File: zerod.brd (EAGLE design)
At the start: 100 x 80 mm, 34 parts, among them IC1 NE5532N, IC2 LM3914N, Q1 2N3906

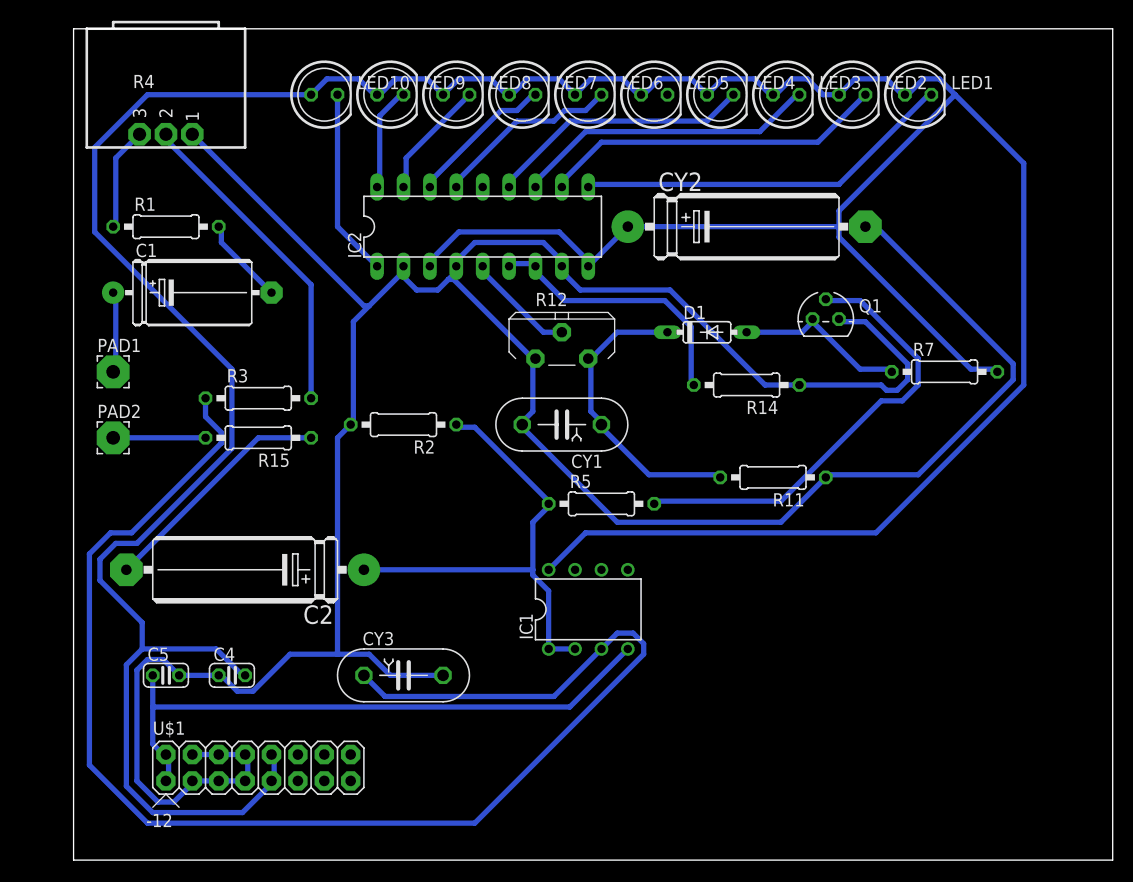
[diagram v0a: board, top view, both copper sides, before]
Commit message: routed board to match updated schematic
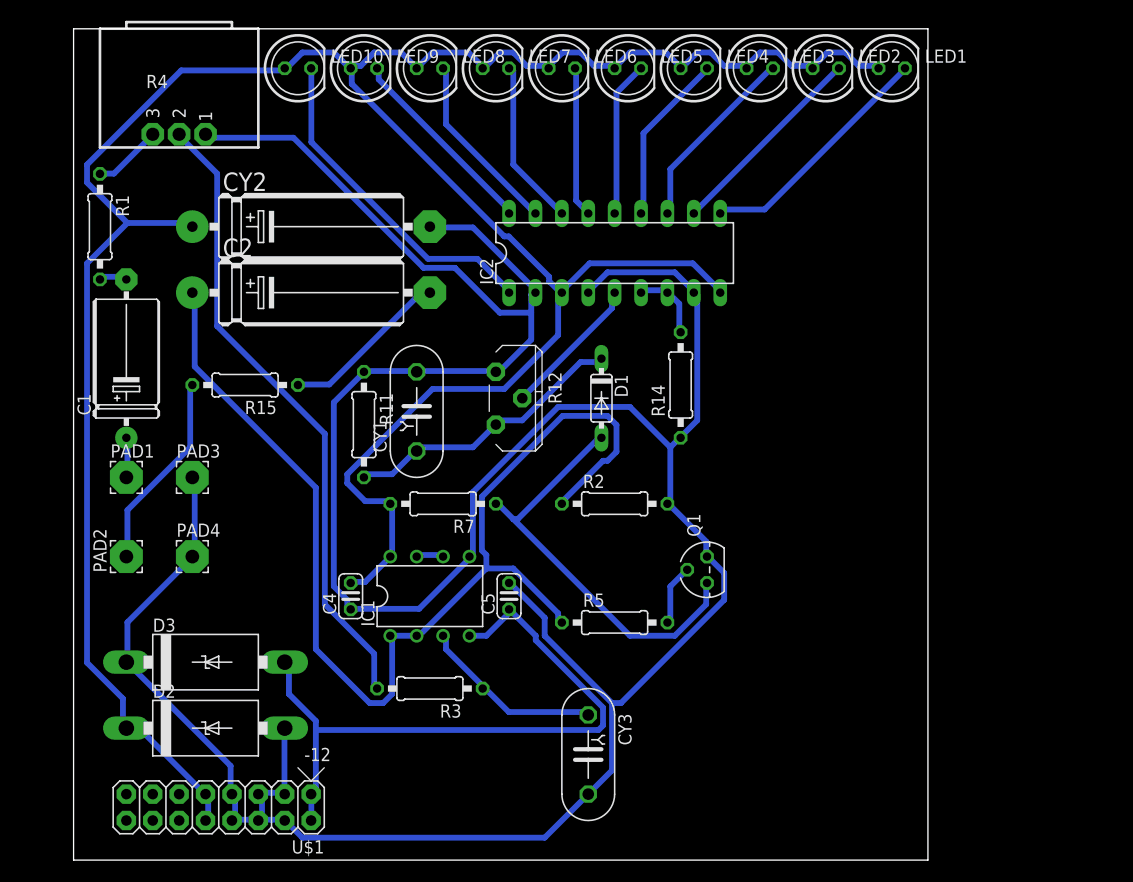
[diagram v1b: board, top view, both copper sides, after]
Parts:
- added D2, D3: 1N5908, diode:C4111-15
- added PAD3: input, wirepad:3,17/1,3
- added PAD4: output, wirepad:3,17/1,3
- moved R7 49.9 mm to (35.6, 34.3), turned to 180 degrees
- moved CY2 41.9 mm to (22.9, 61.0)
- moved R11 39.7 mm to (27.9, 41.9), turned to 270 degrees
- moved C5 33.9 mm to (41.9, 25.4), turned to 90 degrees
- moved R3 32.5 mm to (34.3, 16.5), turned to 180 degrees
- moved C2 27.4 mm to (22.9, 54.6), turned to 0 degrees
- moved Q1 26.7 mm to (61.0, 27.9), turned to 90 degrees
- moved R2 21.7 mm to (52.1, 34.3), turned to 0 degrees
- moved CY3 19.3 mm to (49.5, 10.2), turned to 270 degrees
- moved IC1 15.3 mm to (34.3, 25.4)
- moved CY1 14.0 mm to (33.0, 43.2), turned to 90 degrees
- moved C4 13.7 mm to (26.7, 25.4), turned to 90 degrees
- moved IC2 13.0 mm to (52.1, 58.4)
- moved D1 12.0 mm to (50.8, 44.5), turned to 270 degrees
- moved PAD2 11.5 mm to (5.08, 29.2), turned to 90 degrees
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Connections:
- new net N$24: IC1.6, IC1.7
- net +12V: now also D2.C
- net -12V: now also D3.A
- net GNDA: now also D2.A, D3.C, IC1.5, PAD3.1, PAD4.1
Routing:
- net N$6: track 136.5 -> 18.0 mm
- net +12V: track 370.8 -> 264.4 mm
- net N$5: track 46.2 -> 110.2 mm
- net N$9: track 44.1 -> 6.02 mm
- net N$7: track 31.4 -> 61.2 mm
- net N$15: track 16.8 -> 40.5 mm
- net GNDA: track 295.3 -> 316.4 mm
- net N$14: track 26.5 -> 7.11 mm
- net N$18: track 0.00 -> 15.0 mm
- net N$23: track 18.1 -> 32.2 mm
- net N$13: track 33.2 -> 19.8 mm
- net N$11: track 36.7 -> 23.6 mm
- net N$16: track 29.4 -> 18.2 mm
- net N$8: track 8.89 -> 19.1 mm
- net N$22: track 10.1 -> 19.2 mm
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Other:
- board size 100 x 80 mm -> 82.2 x 80 mm

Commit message: redid layout
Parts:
- moved CY3 31.1 mm to (19.1, 16.5), turned to 0 degrees
- moved R3 26.1 mm to (15.2, 34.3), turned to 90 degrees
- moved R5 22.2 mm to (61.0, 43.2)
- moved R7 21.6 mm to (45.7, 53.3)
- moved Q1 20.3 mm to (61.0, 48.3), turned to 270 degrees
- moved R11 18.9 mm to (45.7, 48.3), turned to 0 degrees
- moved CY1 13.5 mm to (43.2, 34.3), turned to 180 degrees
- moved CY2 12.6 mm to (31.8, 52.1), turned to 90 degrees
- moved PAD3 10.8 mm to (3.81, 29.2)
- moved R14 9.25 mm to (61.0, 54.6), turned to 180 degrees
- moved D2 8.89 mm to (12.7, 21.6)
- moved PAD2 8.52 mm to (8.89, 36.8)
- moved D3 7.62 mm to (12.7, 11.4)
- moved C5 6.48 mm to (48.3, 24.1)
- moved R2 6.48 mm to (58.4, 33.0), turned to 90 degrees
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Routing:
- net GNDA: track 316.4 -> 375.0 mm
- net N$5: track 110.2 -> 71.9 mm
- net N$15: track 40.5 -> 11.7 mm
- net N$7: track 61.2 -> 33.9 mm
- net -12V: track 64.7 -> 40.9 mm
- net N$6: track 18.0 -> 41.1 mm
- net +12V: track 264.4 -> 253.3 mm
- net N$12: track 27.7 -> 18.1 mm
- net N$8: track 19.1 -> 11.5 mm
- net N$23: track 32.2 -> 26.4 mm
- net N$3: track 16.4 -> 10.8 mm
- net N$1: track 3.89 -> 7.93 mm
- net N$10: track 13.9 -> 17.9 mm
- net N$20: track 16.1 -> 12.3 mm
- net N$21: track 17.7 -> 13.8 mm
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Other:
- board size 82.2 x 80 mm -> 87.3 x 80 mm

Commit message: redid layout for 100%
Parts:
- moved D2 2.84 mm to (15.2, 22.9)
- moved D3 2.54 mm to (15.2, 11.4)
- moved C1 2.54 mm to (10.2, 50.8)
- moved R1 2.54 mm to (5.08, 61.0)
- moved PAD1 2.54 mm to (6.35, 36.8)
- moved PAD3 2.54 mm to (6.35, 29.2)
- moved PAD2 2.54 mm to (11.4, 36.8)
- moved PAD4 2.54 mm to (11.4, 29.2)
- moved R3 1.27 mm to (16.5, 34.3)
- moved U$1 1.27 mm to (17.8, 5.08)
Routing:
- net GNDA: track 375.0 -> 349.9 mm
- net +12V: track 253.3 -> 230.5 mm
- net N$5: track 71.9 -> 80.9 mm
- net N$6: track 41.1 -> 38.3 mm
- net -12V: track 40.9 -> 38.3 mm
- net N$4: track 6.66 -> 4.86 mm
- net N$8: track 11.5 -> 10.5 mm
- net N$7: track 33.9 -> 33.4 mm
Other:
- board size 87.3 x 80 mm -> 82.2 x 80 mm
